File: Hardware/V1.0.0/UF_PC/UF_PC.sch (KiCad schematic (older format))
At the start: 3 parts

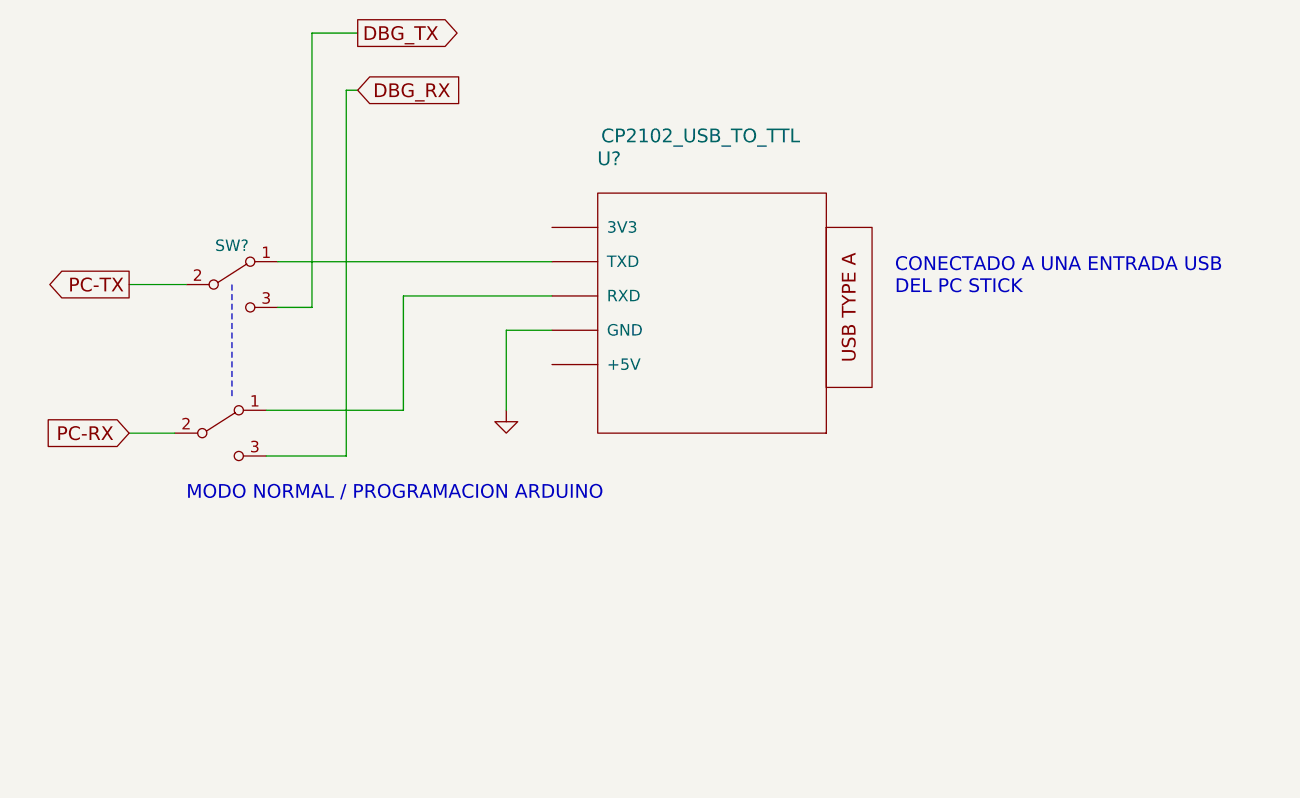
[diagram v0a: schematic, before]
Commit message: Actualizado proceso ON/OFF
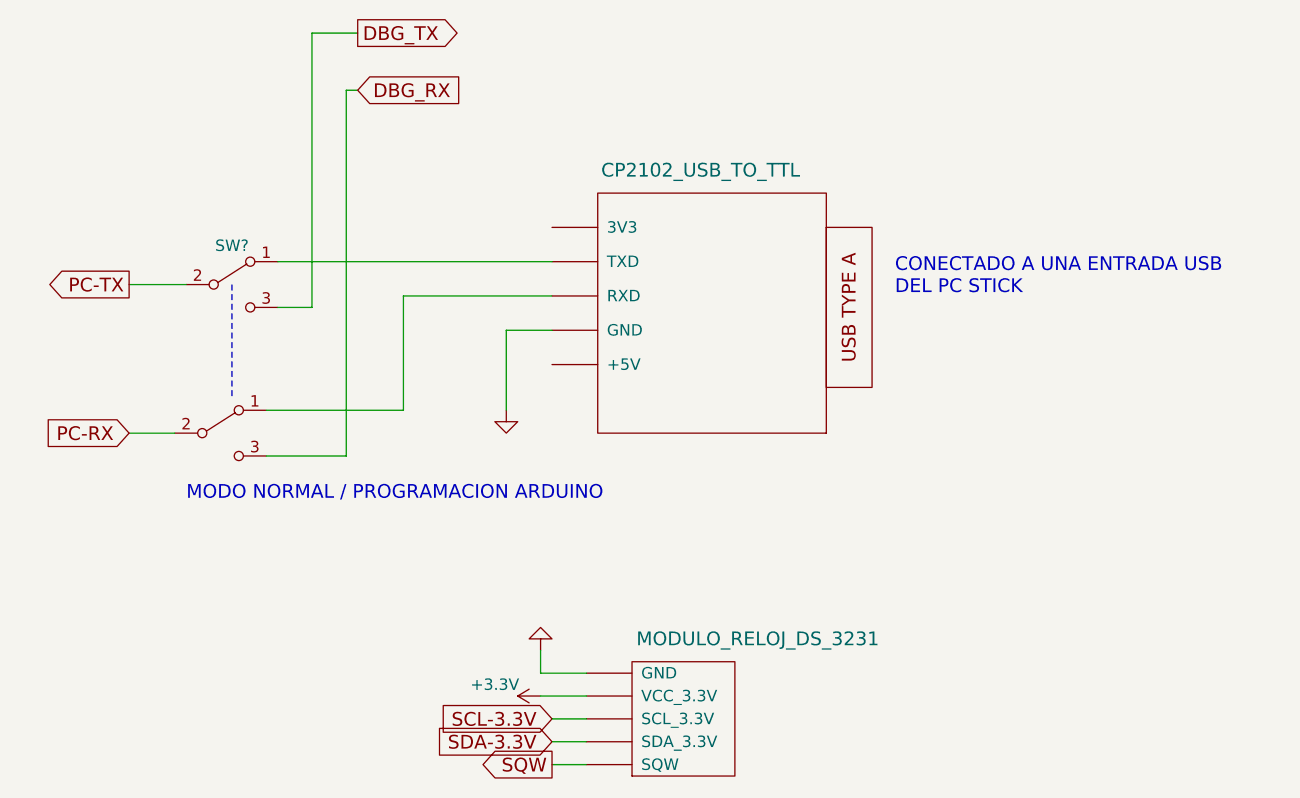
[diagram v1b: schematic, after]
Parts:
- added U?: MODULO_RELOJ_DS_3231, symbol MODULO_RELOJ_DS_3231
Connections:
- net GND: now also U?.~ (VCC_3.3V)
- new net +3V3: U?.~ (VCC_3.3V)
- new net SCL-3.3V: U?.~ (VCC_3.3V)
- new net SDA-3.3V: U?.~ (VCC_3.3V)
- new net SQW: U?.~ (VCC_3.3V)
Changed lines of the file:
@@
 LIBS:Baphomet_Libreria
 LIBS:switches
+LIBS:UF_PC-cache
 EELAYER 25 0
 EELAYER END
@@
 Rev "1.0"
 Comp "iROB-EA_VS_2021_UF_PC"
-Comment1 "Subsistema PC"
+Comment1 "Subsistema PC y circuitos miscelaneos"
 Comment2 ""
 Comment3 ""
@@
 U 1 1 619BE658
 P 8100 1500
-F 0 "U?" H 8250 1550 60  0000 C CNN
-F 1 "CP2102_USB_TO_TTL" H 8650 1650 60  0000 C CNN
+F 0 "U?" H 8250 1550 60  0001 C CNN
+F 1 "CP2102_USB_TO_TTL" H 8650 1500 60  0000 C CNN
 F 2 "" H 8100 1500 60  0001 C CNN
 F 3 "" H 8100 1500 60  0001 C CNN
@@
 Text Notes 6400 2950 0    60   ~ 0
 MODO NORMAL / PROGRAMACION ARDUINO
+$Comp
+L GND #PWR?
+U 1 1 619F8563
+P 7950 3600
+F 0 "#PWR?" H 7950 3350 50  0001 C CNN
+F 1 "GND" H 7950 3450 50  0001 C CNN
+F 2 "" H 7950 3600 50  0000 C CNN
+F 3 "" H 7950 3600 50  0000 C CNN
+	1    7950 3600
+	-1   0    0    1
+$EndComp
+Wire Wire Line
+	8150 3700 7950 3700
+$Comp
+L +3.3V #PWR?
+U 1 1 619F85BA
+P 7950 3800
+F 0 "#PWR?" H 7950 3650 50  0001 C CNN
+F 1 "+3.3V" V 8000 4000 50  0000 C CNN
+F 2 "" H 7950 3800 50  0000 C CNN
+F 3 "" H 7950 3800 50  0000 C CNN
+	1    7950 3800
+	0    -1   -1   0
+$EndComp
+Wire Wire Line
+	7950 3700 7950 3600
+Wire Wire Line
+	7950 3800 8150 3800
+Text GLabel 8000 3900 0    60   Input ~ 0
+SCL-3.3V
+Wire Wire Line
+	8000 3900 8150 3900
+Text GLabel 8000 4000 0    60   Input ~ 0
+SDA-3.3V
+Wire Wire Line
+	8000 4000 8150 4000
+Text GLabel 8000 4100 0    60   Output ~ 0
+SQW
+Wire Wire Line
+	8000 4100 8150 4100
+$Comp
+L MODULO_RELOJ_DS_3231 U?
+U 1 1 619F8BC6
+P 8300 3550
+F 0 "U?" H 8400 3500 60  0001 C CNN
+F 1 "MODULO_RELOJ_DS_3231" H 8900 3550 60  0000 C CNN
+F 2 "" H 8300 3550 60  0001 C CNN
+F 3 "" H 8300 3550 60  0001 C CNN
+	1    8300 3550
+	1    0    0    -1
+$EndComp
 $EndSCHEMATC
